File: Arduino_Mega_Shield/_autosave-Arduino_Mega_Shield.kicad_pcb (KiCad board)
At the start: 2 copper layers, 101.6 x 53.4 mm, 37 parts, among them J1 Conn_01x04, J10 Conn_01x02, J11 Conn_01x02, J12 Conn_01x02, J13 Conn_01x02, J14 Conn_01x02, J15 Motor Driver Connector, J16 Motor Driver Connector, J17 Motor Driver Connector, J18 Motor Driver Connector, J2 Conn_01x04, J3 Conn_01x04, J4 Conn_01x04, J5 Conn_01x02, J6 Conn_01x02, J7 Conn_01x02, J8 Conn_01x02, J9 Conn_01x02

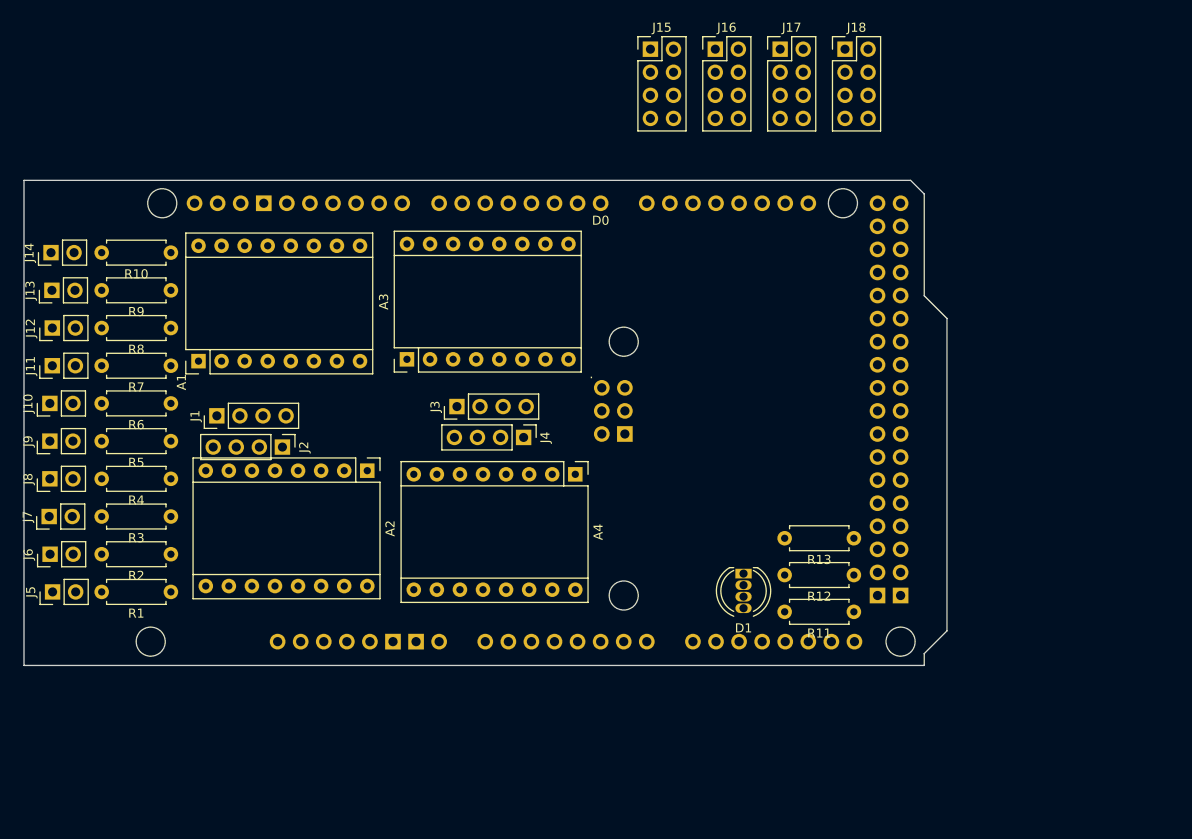
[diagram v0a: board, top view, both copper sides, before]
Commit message: Update KiCad PCB (Pololu A4988) and ESP32 code
Replace Arduino Mega shield footprint with a Pololu A4988 breakout footprint and reorganize PCB item positions/annotations (silkscreen, fab, footprint properties, net index adjustments). Add several Arduino_Mega_Shield backup zip files. Also include changes to ESP-32 embedded code (src/main.cpp and src/motor_constants.hpp) — likely motor/driver-related updates to match the hardware footprint changes.
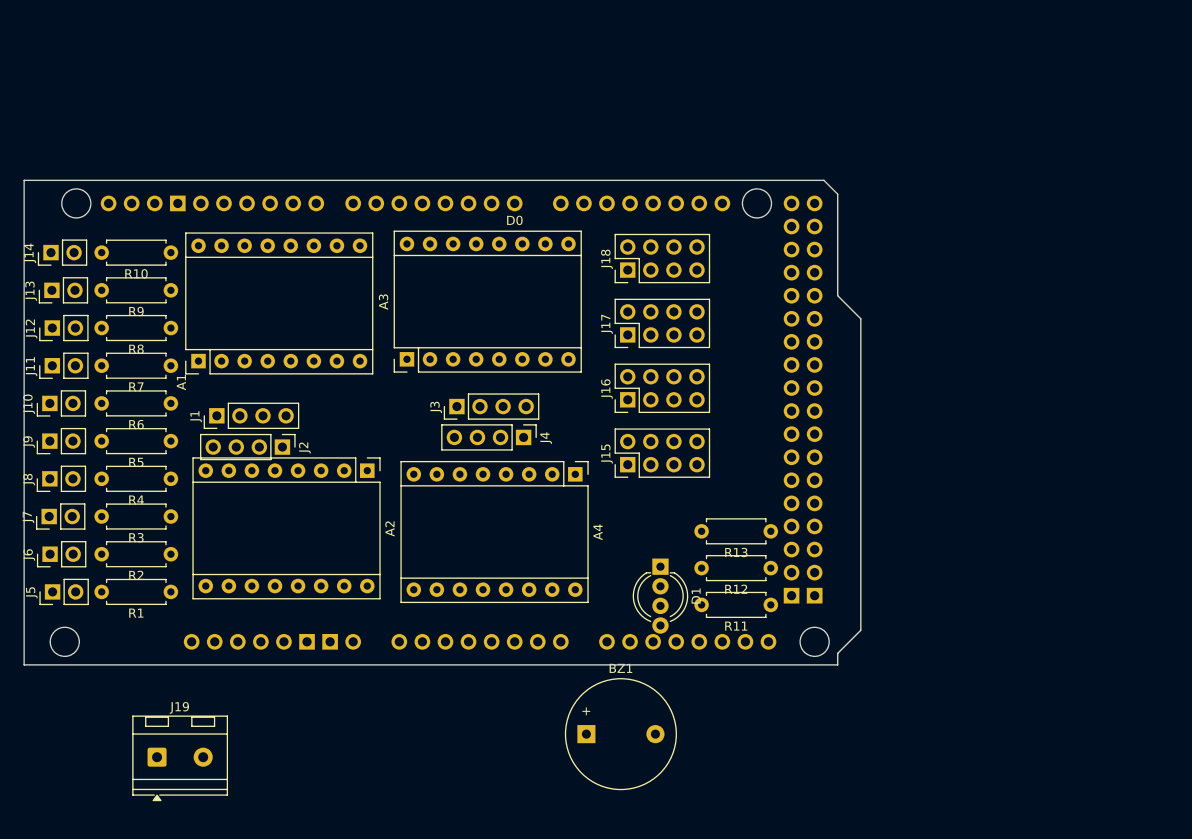
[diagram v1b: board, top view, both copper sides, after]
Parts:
- added BZ1: Buzzer, Buzzer_Beeper:Buzzer_12x9.5RM7.6, F.Cu at (164.6, 124.5)
- added J19: Screw_Terminal_01x02, TerminalBlock_RND:TerminalBlock_RND_205-00232_1x02_P5.08mm_Horizontal, F.Cu at (117.3, 127.0)
- D1: value LED_RGBK -> LED_RKGB; footprint LED_THT:LED_D5.0mm-4_RGB -> LED_THT:LED_D5.0mm-4_RGB_Wide_Pins
- moved J15 45.8 mm to (169.2, 94.8), turned to 90 degrees
- moved J16 39.8 mm to (169.2, 87.7), turned to 90 degrees
- moved J17 35.7 mm to (169.2, 80.5), turned to 90 degrees
- moved J18 34.1 mm to (169.2, 73.4), turned to 90 degrees
- moved A5 9.46 mm to (93.2, 116.8)
- moved D1 9.18 mm to (172.8, 106.0)
- moved R11 9.18 mm to (184.9, 110.2)
- moved R12 9.18 mm to (184.9, 106.2)
- moved R13 9.18 mm to (184.9, 102.1)
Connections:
- D1 pad 2: Net-(D1-GA) -> GND
- D1 pad 3: Net-(D1-BA) -> Net-(D1-GA)
- D1 pad 4: GND -> Net-(D1-BA)
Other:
- board size 101.6 x 53.4 mm -> 92.1 x 53.3 mm

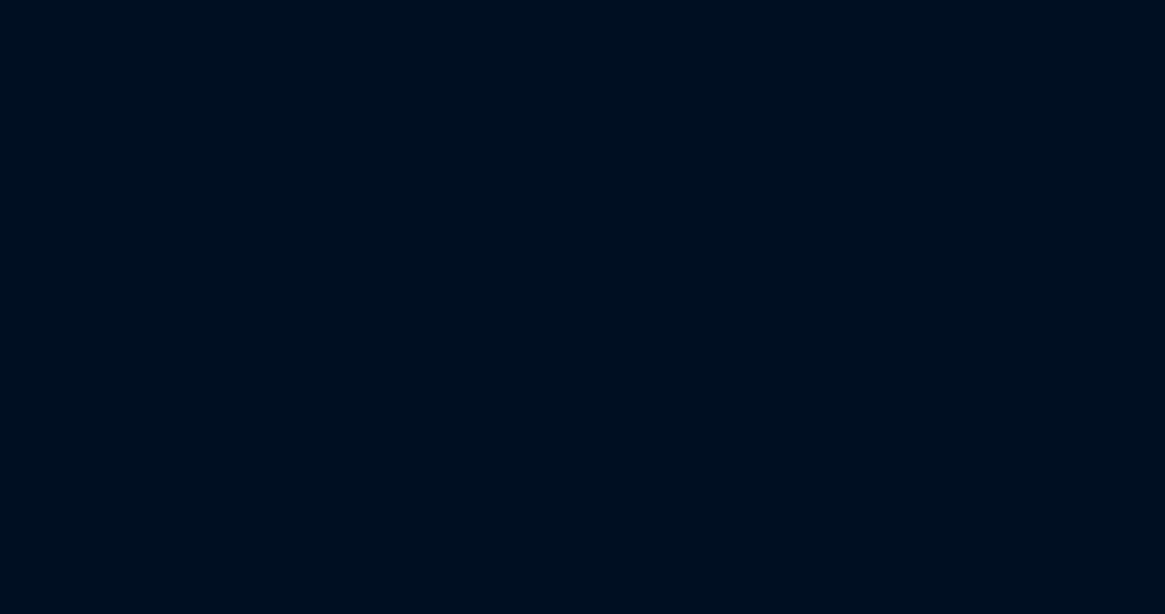
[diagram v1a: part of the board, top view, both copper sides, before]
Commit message: Update code to analyse image and rename pictures
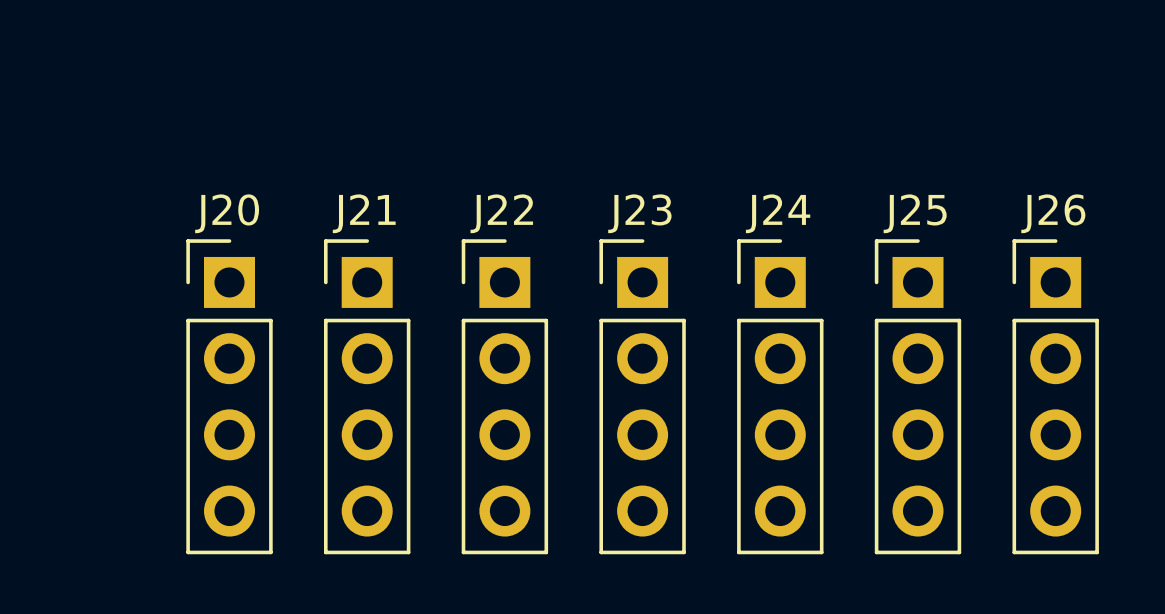
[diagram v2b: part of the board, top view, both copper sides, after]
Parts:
- added J20: JOYSTICK, Connector_PinHeader_2.54mm:PinHeader_1x04_P2.54mm_Vertical, F.Cu at (200.0, 125.0)
- added J21: I2C CONNECTOR, Connector_PinHeader_2.54mm:PinHeader_1x04_P2.54mm_Vertical, F.Cu at (204.6, 125.0)
- added J22: ENCODER1, Connector_PinHeader_2.54mm:PinHeader_1x04_P2.54mm_Vertical, F.Cu at (209.2, 125.0)
- added J23: ENCODER2, Connector_PinHeader_2.54mm:PinHeader_1x04_P2.54mm_Vertical, F.Cu at (213.8, 125.0)
- added J24: ENCODER3, Connector_PinHeader_2.54mm:PinHeader_1x04_P2.54mm_Vertical, F.Cu at (218.4, 125.0)
- added J25: ENCODER4, Connector_PinHeader_2.54mm:PinHeader_1x04_P2.54mm_Vertical, F.Cu at (223.0, 125.0)
- added J26: I2C CONNECTOR, Connector_PinHeader_2.54mm:PinHeader_1x04_P2.54mm_Vertical, F.Cu at (227.6, 125.0)
- J10: value Conn_01x02 -> SW10
- J11: value Conn_01x02 -> SW6
- J12: value Conn_01x02 -> SW7
- J13: value Conn_01x02 -> SW8
- J14: value Conn_01x02 -> SW9
- J5: value Conn_01x02 -> SW5
- J6: value Conn_01x02 -> SW1
- J7: value Conn_01x02 -> SW2
- J8: value Conn_01x02 -> SW3
- J9: value Conn_01x02 -> SW4
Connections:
- net Net-(J10-Pin_2) renamed SW10
- net Net-(J11-Pin_2) renamed SW6
- net Net-(J12-Pin_2) renamed SW7
- net Net-(J13-Pin_2) renamed SW8
- net Net-(J14-Pin_2) renamed SW9
- net Net-(J5-Pin_2) renamed SW5
- net Net-(J6-Pin_2) renamed SW1
- net Net-(J7-Pin_2) renamed SW2
- net Net-(J8-Pin_2) renamed SW3
- net Net-(J9-Pin_2) renamed SW4
- A5 pad 5V1: unconnected-(A5-5V-Pad5V1) -> +5V
- A5 pad 5V3: unconnected-(A5-5V-Pad5V3) -> +5V
- A5 pad 5V4: unconnected-(A5-5V-Pad5V4) -> +5V
- A5 pad A0: unconnected-(A5-PadA0) -> VRX
- A5 pad A1: unconnected-(A5-PadA1) -> VRY
- A5 pad D10: unconnected-(A5-PadD10) -> RPWM3
- A5 pad D11: unconnected-(A5-PadD11) -> LPWM3
- A5 pad D12: unconnected-(A5-PadD12) -> RPWM4
- A5 pad D13: unconnected-(A5-PadD13) -> LPWM4
- A5 pad D20: unconnected-(A5-D20/SDA-PadD20) -> SDA
- A5 pad D21: unconnected-(A5-D21/SCL-PadD21) -> SCL
- A5 pad D22: unconnected-(A5-PadD22) -> R_EN1
- A5 pad D23: unconnected-(A5-PadD23) -> L_EN1
- A5 pad D24: unconnected-(A5-PadD24) -> R_EN2
- A5 pad D25: unconnected-(A5-PadD25) -> L_EN2
- A5 pad D26: unconnected-(A5-PadD26) -> R_EN3
- A5 pad D27: unconnected-(A5-PadD27) -> L_EN3
- A5 pad D28: unconnected-(A5-PadD28) -> R_EN4
- A5 pad D29: unconnected-(A5-PadD29) -> L_EN4
- A5 pad D30: unconnected-(A5-PadD30) -> R_IS1
- A5 pad D31: unconnected-(A5-PadD31) -> L_IS1
- A5 pad D32: unconnected-(A5-PadD32) -> R_IS2
- A5 pad D33: unconnected-(A5-PadD33) -> L_IS2
- A5 pad D34: unconnected-(A5-PadD34) -> R_IS3
- A5 pad D35: unconnected-(A5-PadD35) -> L_IS3
- A5 pad D36: unconnected-(A5-PadD36) -> R_IS4
- A5 pad D37: unconnected-(A5-PadD37) -> L_IS4
- A5 pad D6: unconnected-(A5-PadD6) -> RPWM1
- A5 pad D7: unconnected-(A5-PadD7) -> LPWM1
- A5 pad D8: unconnected-(A5-PadD8) -> RPWM2
- A5 pad D9: unconnected-(A5-PadD9) -> LPWM2
- A5 pad GND1: unconnected-(A5-GND-PadGND1) -> GND
- A5 pad GND2: unconnected-(A5-GND-PadGND2) -> GND
- A5 pad GND3: unconnected-(A5-GND-PadGND3) -> GND
- A5 pad GND5: unconnected-(A5-GND-PadGND5) -> GND
- A5 pad GND6: unconnected-(A5-GND-PadGND6) -> GND
- A5 pad SCL: unconnected-(A5-PadSCL) -> SCL
- A5 pad SDA: unconnected-(A5-PadSDA) -> SDA
- A5 pad VIN: unconnected-(A5-PadVIN) -> +12V
- BZ1 pad 1: unconnected-(BZ1-+-Pad1) -> BUZZER
- J15 pad 1: unconnected-(J15-Pin_1-Pad1) -> RPWM1
- J15 pad 2: unconnected-(J15-Pin_2-Pad2) -> LPWM1
- J15 pad 3: unconnected-(J15-Pin_3-Pad3) -> R_EN1
- J15 pad 4: unconnected-(J15-Pin_4-Pad4) -> L_EN1
- J15 pad 5: unconnected-(J15-Pin_5-Pad5) -> R_IS1
- J15 pad 6: unconnected-(J15-Pin_6-Pad6) -> L_IS1
- J15 pad 7: unconnected-(J15-Pin_7-Pad7) -> +5V
- J15 pad 8: unconnected-(J15-Pin_8-Pad8) -> GND
- J16 pad 1: unconnected-(J16-Pin_1-Pad1) -> RPWM2
- J16 pad 2: unconnected-(J16-Pin_2-Pad2) -> LPWM2
- J16 pad 3: unconnected-(J16-Pin_3-Pad3) -> R_EN2
- J16 pad 4: unconnected-(J16-Pin_4-Pad4) -> L_EN2
- J16 pad 5: unconnected-(J16-Pin_5-Pad5) -> R_IS2
- J16 pad 6: unconnected-(J16-Pin_6-Pad6) -> L_IS2
- J16 pad 7: unconnected-(J16-Pin_7-Pad7) -> +5V
- J16 pad 8: unconnected-(J16-Pin_8-Pad8) -> GND
- J17 pad 1: unconnected-(J17-Pin_1-Pad1) -> RPWM3
- J17 pad 2: unconnected-(J17-Pin_2-Pad2) -> LPWM3
- J17 pad 3: unconnected-(J17-Pin_3-Pad3) -> R_EN3
- J17 pad 4: unconnected-(J17-Pin_4-Pad4) -> L_EN3
- J17 pad 5: unconnected-(J17-Pin_5-Pad5) -> R_IS3
- J17 pad 6: unconnected-(J17-Pin_6-Pad6) -> L_IS3
- J17 pad 7: unconnected-(J17-Pin_7-Pad7) -> +5V
- J17 pad 8: unconnected-(J17-Pin_8-Pad8) -> GND
- J18 pad 1: unconnected-(J18-Pin_1-Pad1) -> RPWM4
- J18 pad 2: unconnected-(J18-Pin_2-Pad2) -> LPWM4
- J18 pad 3: unconnected-(J18-Pin_3-Pad3) -> R_EN4
- J18 pad 4: unconnected-(J18-Pin_4-Pad4) -> L_EN4
- J18 pad 5: unconnected-(J18-Pin_5-Pad5) -> R_IS4
- J18 pad 6: unconnected-(J18-Pin_6-Pad6) -> L_IS4
- J18 pad 7: unconnected-(J18-Pin_7-Pad7) -> +5V
- J18 pad 8: unconnected-(J18-Pin_8-Pad8) -> GND
- J19 pad 1: unconnected-(J19-Pin_1-Pad1) -> +12V
- J19 pad 2: unconnected-(J19-Pin_2-Pad2) -> GND
- R11 pad 1: unconnected-(R11-Pad1) -> LEDB
- R12 pad 1: unconnected-(R12-Pad1) -> LEDG
- R13 pad 1: unconnected-(R13-Pad1) -> LEDR
